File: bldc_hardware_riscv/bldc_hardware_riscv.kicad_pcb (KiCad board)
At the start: 4 copper layers, 80 x 60 mm, 137 parts, among them J1 USB_B_Micro Vertical, J2 2.00mm JST 6Pin, J3 2.00mm JST 6Pin, J4 Screw_Terminal_01x04, J5 Screw_Terminal_01x03, Q1 80V/200A, Q2 80V/200A, Q3 80V/200A, Q4 80V/200A, Q5 80V/200A, Q6 80V/200A, SW1 B3U-1000P, U1 CH32V307VCT6, U101 MAX9919, U102 MAX9919, U103 MAX9919, U2 XL1509-3.3 XLSEMI, U3 EG2134 EG Micro, U4 XL7046 XLSEMI, U5 RT9058-50GVL Richtek, U6 RT9058-50GVL Richtek, U7 SN65HVD230, U8 CH9141K, X1 CON-T, X2 CON-T, X3 CON-T, X4 CON-T, X5 CON-T, Y1 8MHz 3225, Y2 32MHz 3225

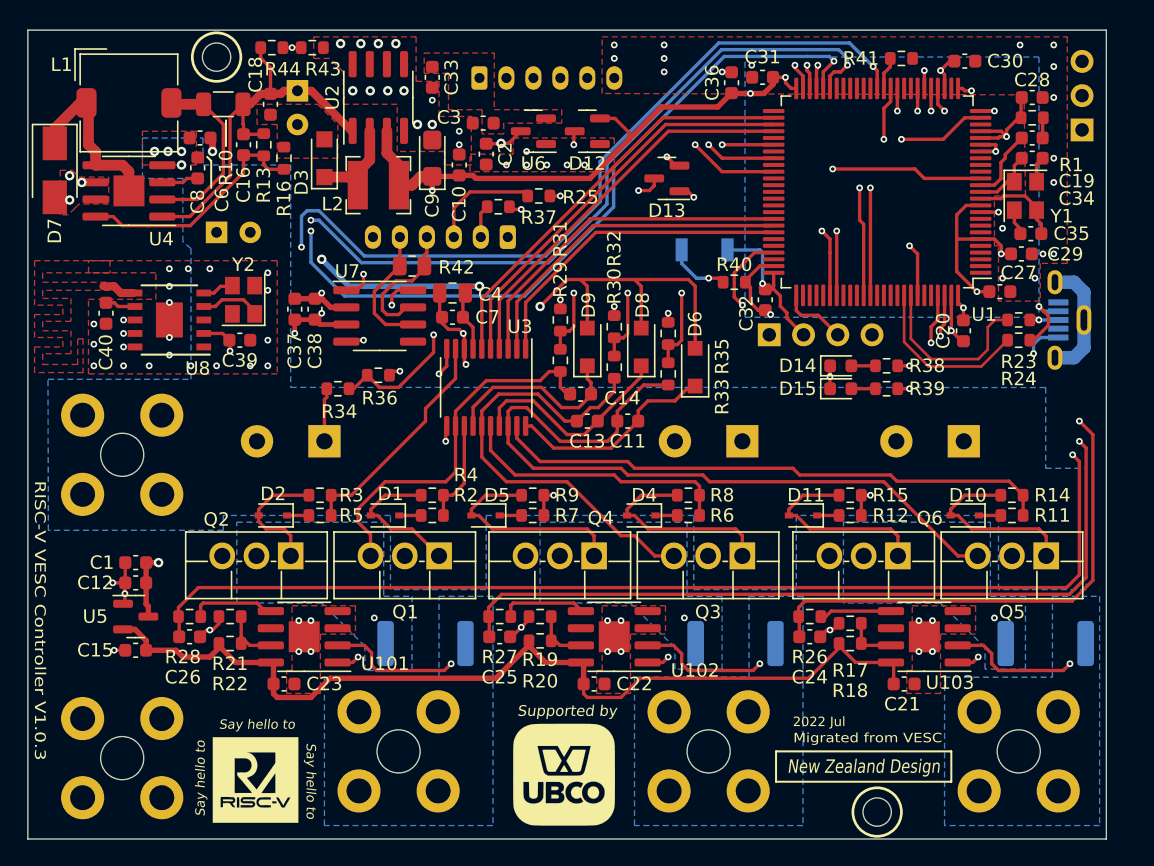
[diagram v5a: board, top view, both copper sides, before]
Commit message: use hall current sensor (60A limit), use keystone terminal, support up to 120V input
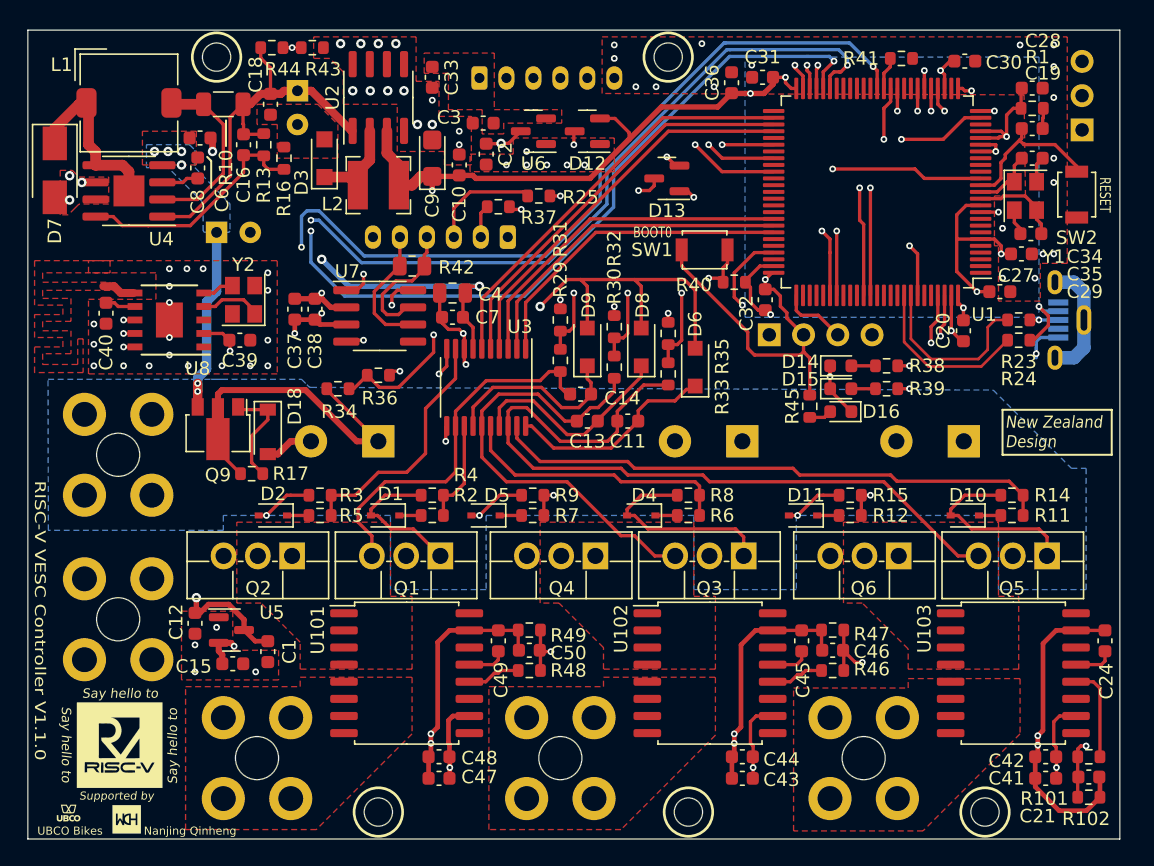
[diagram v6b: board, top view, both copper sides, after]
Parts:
- removed C22, C23: 2.2uF, Capacitor_SMD:C_0603_1608Metric
- removed C25, C26: 10nF, Capacitor_SMD:C_0603_1608Metric
- removed R103: 0.0003, Resistor_SMD:R_2512_6332Metric
- removed R18, R20, R22: 4K3, Resistor_SMD:R_0603_1608Metric
- removed R19, R21: 2K2, Resistor_SMD:R_0603_1608Metric
- removed R26, R27, R28: 100, Resistor_SMD:R_0603_1608Metric
- added C41: 2.2uF, Capacitor_SMD:C_0603_1608Metric, F.Cu at (155.5, 135.5)
- added C42: 0.1uF, Capacitor_SMD:C_0603_1608Metric, F.Cu at (155.5, 133.9)
- added C43: 2.2uF, Capacitor_SMD:C_0603_1608Metric, F.Cu at (133.0, 135.5)
- added C44: 0.1uF, Capacitor_SMD:C_0603_1608Metric, F.Cu at (133.0, 133.9)
- added C45: 100pF, Capacitor_SMD:C_0603_1608Metric, F.Cu at (137.4, 125.3)
- added C46: 100pF, Capacitor_SMD:C_0603_1608Metric, F.Cu at (139.7, 126.0)
- added C47: 2.2uF, Capacitor_SMD:C_0603_1608Metric, F.Cu at (110.5, 135.5)
- added C48: 0.1uF, Capacitor_SMD:C_0603_1608Metric, F.Cu at (110.5, 133.9)
- added C49: 100pF, Capacitor_SMD:C_0603_1608Metric, F.Cu at (114.9, 125.3)
- added C50: 100pF, Capacitor_SMD:C_0603_1608Metric, F.Cu at (117.2, 126.0)
- added D16: LED, LED_SMD:LED_0603_1608Metric, F.Cu at (140.3, 108.3)
- added D18: 75V, Diode_SMD:D_SOD-123, F.Cu at (97.8, 109.8)
- added Q9: FCX495, Package_TO_SOT_SMD:SOT-89-3, F.Cu at (94.1, 109.6)
- added R45: 4K3, Resistor_SMD:R_0603_1608Metric, F.Cu at (138.0, 107.9)
- added R46: 2K2, Resistor_SMD:R_0603_1608Metric, F.Cu at (139.7, 127.5)
- added R47: 4K3, Resistor_SMD:R_0603_1608Metric, F.Cu at (139.7, 124.5)
- added R48: 2K2, Resistor_SMD:R_0603_1608Metric, F.Cu at (117.2, 127.5)
- added R49: 4K3, Resistor_SMD:R_0603_1608Metric, F.Cu at (117.2, 124.5)
- added SW2: B3U-1000P, Button_Switch_SMD:SW_SPST_B3U-1000P, F.Cu at (157.8, 92.2)
- C16, C24: value 10nF -> 100pF
- C21: value 2.2uF -> 100pF
- R101: value 0.0003 -> 2K2; footprint Resistor_SMD:R_2512_6332Metric -> Resistor_SMD:R_0603_1608Metric; moved to F.Cu
- R102: value 0.0003 -> 4K3; footprint Resistor_SMD:R_2512_6332Metric -> Resistor_SMD:R_0603_1608Metric; moved to F.Cu
- R17: value 2K2 -> 150K
- SW1: moved to F.Cu
- U101, U102, U103: value MAX9919 -> MT9222WT-65BR5; footprint BLDC_Library:HSOP-8-1EP_3.9x4.9mm_P1.27mm_EP2.3x2.3mm -> Package_SO:SOIC-16W_7.5x10.3mm_P1.27mm
- X1, X2, X3, X4, X5: value CON-T -> Keystone-7693; footprint BLDC_Library:Wuerth_REDCUBE-THR_WP-THRBU_74650073_THR -> BLDC_Library:Keystone-7693
- moved R101 49.9 mm to (158.7, 133.9), turned to 180 degrees
- moved R17 45.8 mm to (96.6, 112.9), turned to 180 degrees
- moved R102 28.6 mm to (158.7, 136.9)
- moved C24 21.9 mm to (159.9, 125.3), turned to 90 degrees
- moved C21 15.3 mm to (158.7, 135.4)
- moved C1 11.8 mm to (97.8, 126.1), turned to -90 degrees
- moved X5 11.5 mm to (142.0, 134.0)
- moved X4 11.0 mm to (119.5, 134.0)
- moved X3 10.5 mm to (97.0, 134.0)
- moved X2 10.3 mm to (86.7, 123.7)
- moved U101 8.07 mm to (108.1, 127.7), turned to 0 degrees
- moved U102 7.60 mm to (130.6, 127.7), turned to 0 degrees
- moved C15 7.27 mm to (95.2, 127.0), turned to 0 degrees
- moved U5 7.17 mm to (95.1, 124.5)
- moved U103 7.13 mm to (153.1, 127.7), turned to 0 degrees
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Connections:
- C101 pad 1: /Driver/72V -> /Driver/99V
- C102 pad 1: /Driver/72V -> /Driver/99V
- C103 pad 1: /Driver/72V -> /Driver/99V
- C21 pad 1: /Driver/5V -> /AIN_CS3
- C24 pad 1: GND -> Net-(U103-FLT)
- C24 pad 2: /AIN_CS3 -> GND
- C5 pad 1: /Driver/72V -> /Driver/75V
- C6 pad 1: /Driver/72V -> /Driver/75V
- C8 pad 1: /Driver/72V -> /Driver/75V
- Q1 pad 2: /Driver/72V -> /Driver/99V
- Q3 pad 2: /Driver/72V -> /Driver/99V
- Q5 pad 2: /Driver/72V -> /Driver/99V
- R101 pad 1: /Driver/VS1 -> Net-(U103-OUT)
- R101 pad 2: /Driver/PhaseA -> /AIN_CS3
- R102 pad 1: /Driver/VS2 -> /AIN_CS3
- R102 pad 2: /Driver/PhaseB -> GND
- R17 pad 1: GND -> Net-(Q9-B)
- R17 pad 2: Net-(U103-REFIN) -> /Driver/99V
- R34 pad 1: /Driver/72V -> /Driver/99V
- U101 pad 2: /Driver/PhaseA -> /Driver/VS1
- U101 pad 3: GND -> /Driver/VS1
- U101 pad 4: GND -> /Driver/VS1
- U101 pad 5: Net-(U101-OUT) -> /Driver/PhaseA
- U101 pad 6: unconnected-(U101-FB) -> /Driver/PhaseA
- U101 pad 7: Net-(U101-REFIN) -> /Driver/PhaseA
- U101 pad 8: /Driver/5V -> /Driver/PhaseA
- U101 pad 9: GND -> unconnected-(U101-NC)
- U102 pad 2: /Driver/PhaseB -> /Driver/VS2
- U102 pad 3: GND -> /Driver/VS2
- U102 pad 4: GND -> /Driver/VS2
- U102 pad 5: Net-(U102-OUT) -> /Driver/PhaseB
- U102 pad 6: unconnected-(U102-FB) -> /Driver/PhaseB
- U102 pad 7: Net-(U102-REFIN) -> /Driver/PhaseB
- U102 pad 8: /Driver/5V -> /Driver/PhaseB
- U102 pad 9: GND -> unconnected-(U102-NC)
- U103 pad 2: /Driver/PhaseC -> /Driver/VS3
- U103 pad 3: GND -> /Driver/VS3
- U103 pad 4: GND -> /Driver/VS3
- U103 pad 5: Net-(U103-OUT) -> /Driver/PhaseC
- U103 pad 6: unconnected-(U103-FB) -> /Driver/PhaseC
- U103 pad 7: Net-(U103-REFIN) -> /Driver/PhaseC
- U103 pad 8: /Driver/5V -> /Driver/PhaseC
- U103 pad 9: GND -> unconnected-(U103-NC)
- U4 pad 4: /Driver/72V -> /Driver/75V
- X1 pad 1: /Driver/72V -> /Driver/99V
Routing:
- net GND: track 56.2 -> 110.8 mm, vias 94 -> 86
- net /Driver/5V: track 70.5 -> 107.6 mm, vias 0 -> 4
- net /Driver/99V: track 0.00 -> 25.7 mm
- net /AIN_CS1: track 118.6 -> 98.1 mm
- net /AIN_CS2: track 96.0 -> 75.9 mm
- net /Driver/75V: track 0.00 -> 14.5 mm, vias 0 -> 6
- net /3.3V: track 121.0 -> 135.3 mm
- net /Driver/PhaseA: track 9.95 -> 0.00 mm, vias 1 -> 0
- net /Driver/PhaseB: track 9.74 -> 0.00 mm, vias 1 -> 0
- net /Driver/PhaseC: track 9.74 -> 0.00 mm, vias 1 -> 0
- net Net-(Q9-B): track 0.00 -> 7.87 mm
- net /AIN_CS3: track 79.5 -> 72.3 mm
- net /NRST: track 5.36 -> 11.5 mm
- net /Driver/VS3: track 61.4 -> 56.3 mm, vias 2 -> 0
- net /Driver/VS2: track 38.9 -> 33.9 mm, vias 2 -> 0
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- added copper zone on B.Cu, net /Driver/75V
- added copper zone on F.Cu, net /Driver/75V
- added copper zone on B.Cu, net /Driver/99V
- added copper zone on F.Cu, net /Driver/PhaseA
- added copper zone on F.Cu, net /Driver/PhaseB
- added copper zone on F.Cu, net /Driver/PhaseC
- added copper zone on F.Cu, net /Driver/VS1
- added copper zone on F.Cu, net /Driver/VS2
- added copper zone on F.Cu, net /Driver/VS3
- removed copper zone on B.Cu, net /Driver/72V
- removed copper zone on F.Cu, net /Driver/72V
- removed copper zone on B.Cu, net /Driver/PhaseA
- removed copper zone on B.Cu, net /Driver/PhaseB
- removed copper zone on B.Cu, net /Driver/PhaseC
- removed copper zone on B.Cu, net /Driver/VS1
- removed copper zone on B.Cu, net /Driver/VS2
- removed copper zone on B.Cu, net /Driver/VS3
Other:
- board size 80 x 60 mm -> 81 x 60 mm
- board text added: "99V MAX"
- board text added: "Nanjing Qinheng"
- board text added: "RESET"
- board text added: "RISC-V VESC Controller V1.1.0"
- board text added: "UBCO Bikes"
- board text removed: "75V MAX"
- board text removed: "RISC-V VESC Controller V1.0.3"
